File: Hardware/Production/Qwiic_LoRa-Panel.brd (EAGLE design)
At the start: 122.1 x 101.2 mm, 224 parts, among them J1 Qwiic Right Angle, J10 U.FL, J13 Qwiic Right Angle, J14 Qwiic Right Angle, J15 AVR_SPI_PROG_3X2TESTPOINTS, J16 U.FL, J19 Qwiic Right Angle, J2 Qwiic Right Angle, J20 Qwiic Right Angle, J21 AVR_SPI_PROG_3X2TESTPOINTS, J22 U.FL, J4 AVR_SPI_PROG_3X2TESTPOINTS, J5 U.FL, J7 Qwiic Right Angle, J8 Qwiic Right Angle, J9 AVR_SPI_PROG_3X2TESTPOINTS, U1 ATMEGA328P_TQFP, U2 RFM96W, U3 ATMEGA328P_TQFP, U4 RFM96W, U5 ATMEGA328P_TQFP, U6 RFM96W, U7 ATMEGA328P_TQFP, U8 RFM96W, Y1 16MHz, Y2 16MHz, Y3 16MHz, Y4 16MHz

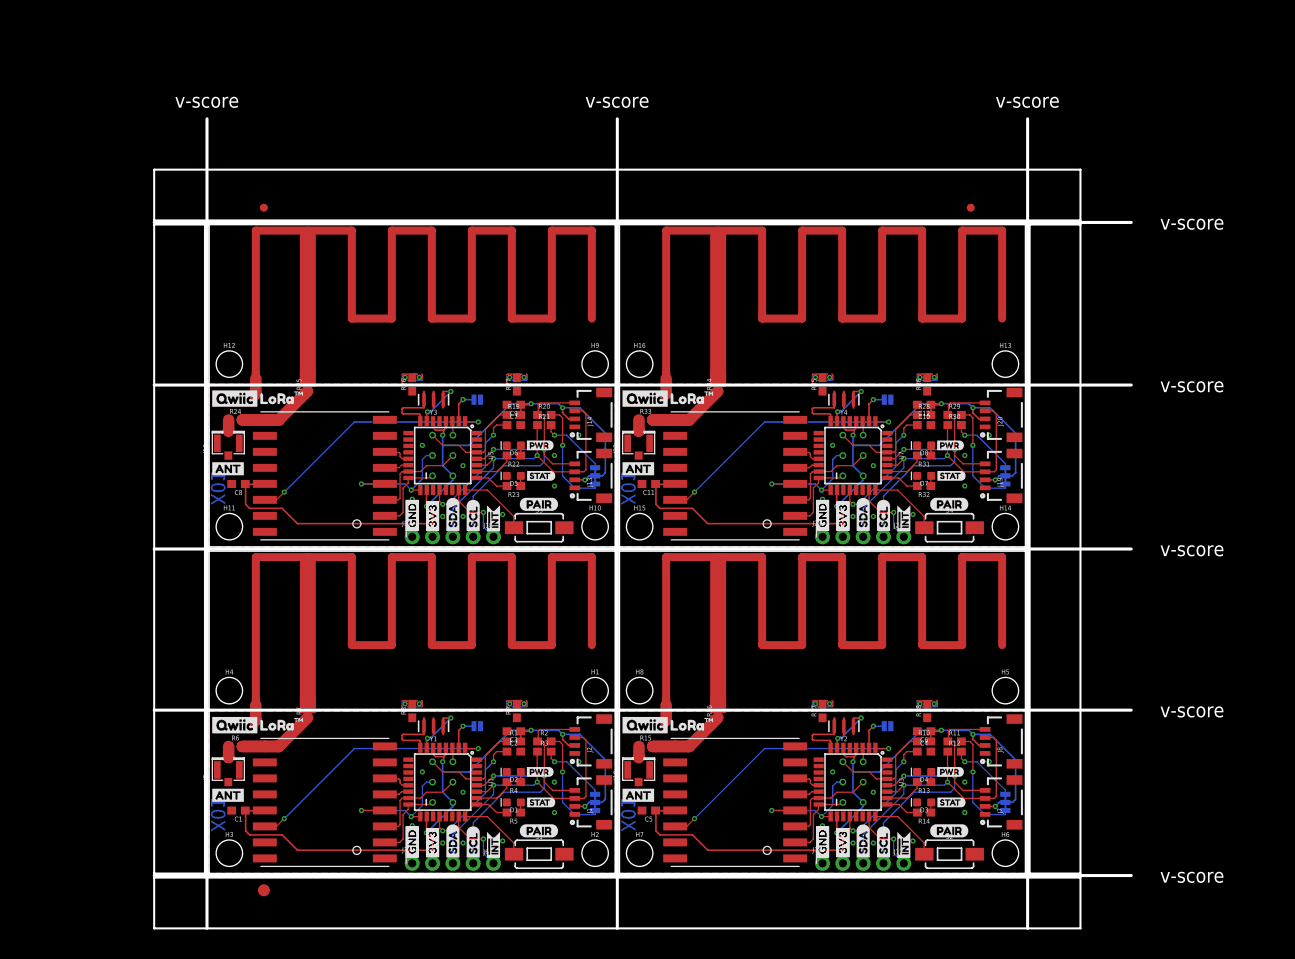
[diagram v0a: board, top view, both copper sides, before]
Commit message: x02
- Trim Antenna
- Silkscreen Changes to Comply with Semtech TM Requirements
- Adjust Mounting Holse to Mount to Qwiic Shield + Arduino R3
- Route DIO1 and DIO2 from RFM95
- Add Serial Debug Testpoints
- Add DNP for Shunt Components
- Add GND Leg Landing for Antenna Footprint
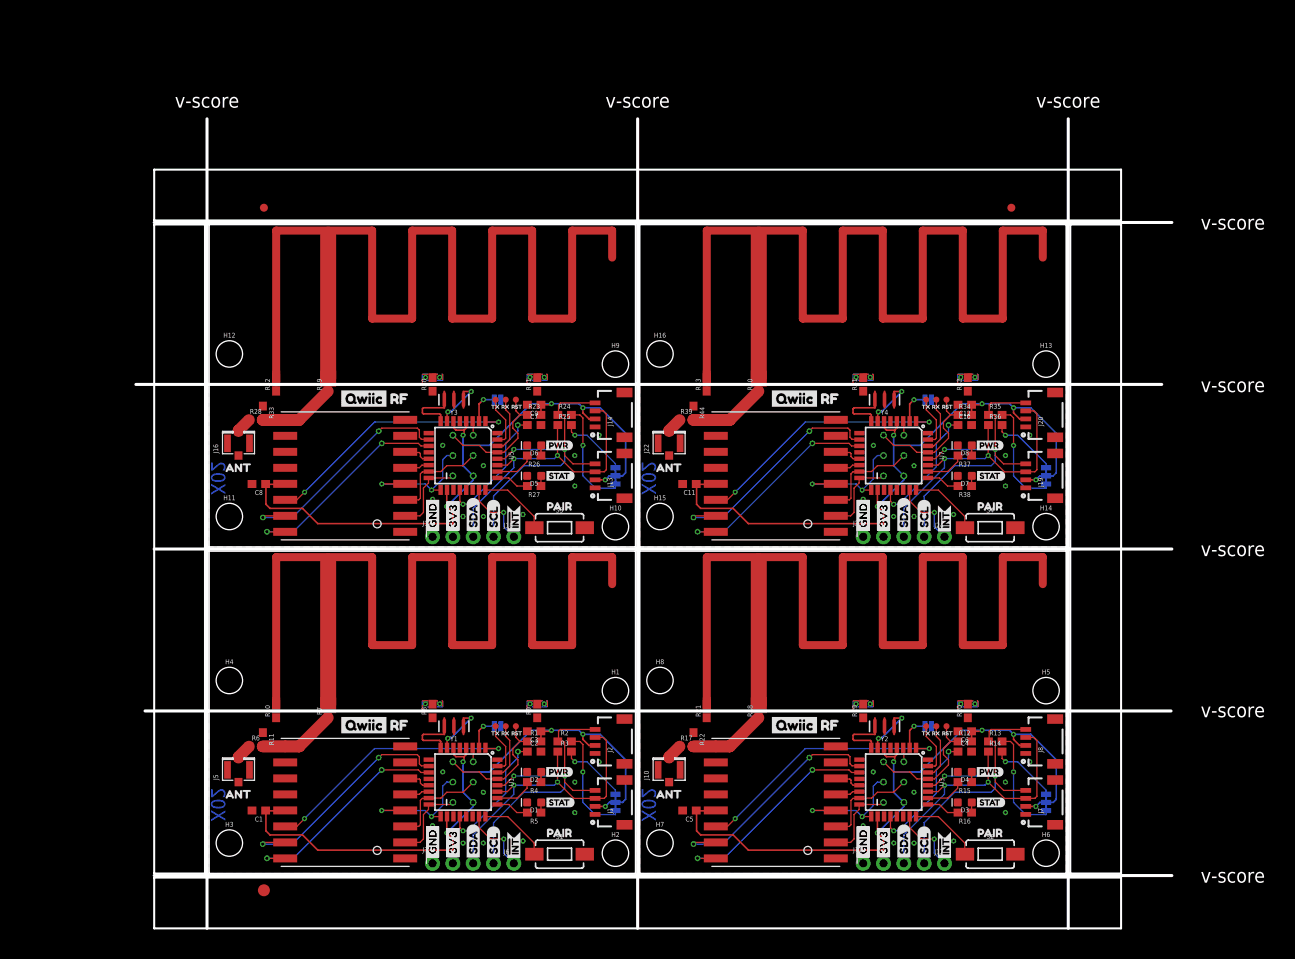
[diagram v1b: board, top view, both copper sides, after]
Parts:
- added R37, R38: 1k, SparkFun-Resistors:0603
- added R39, R44: DNP, SparkFun-Resistors:0603
- added R40, R41, R42, R43: 0, SparkFun-Resistors:0603
- added TP1, TP10, TP11, TP12, TP2, TP3, TP4, TP5, TP6, TP7, TP8, TP9: (no value), SparkFun-Connectors:PAD.03X.03
- added U$102: (no value), Labels:QWIIC-LOGO-SMALL
- added U$103: (no value), lora_mark#PNG (3):LORA_MARK#PNG
- added U$104: (no value), buzzard_labels (30):ANT0
- added U$105: (no value), buzzard_labels (30):PAIR1
- added U$106: (no value), buzzard_labels (32):TX1
- added U$107: (no value), buzzard_labels (32):RX0
- added U$108: (no value), buzzard_labels (32):RST2
- J15, J21, J4, J9: value AVR_SPI_PROG_3X2TESTPOINTS -> AVR_SPI_PROG
- R10, R19: value 10k -> 0
- R11: value 2.2k -> DNP
- R12: value 2.2k -> 10k
- R13, R14: value 1k -> 2.2k
- R15: value DNP -> 1k
- R16, R26, R27: value 0 -> 1k
- R17: value 0 -> DNP
- R20, R21, R29, R30: value 2.2k -> 0
- R22: value 1k -> DNP
- R23: value 1k -> 10k
- R24: value DNP -> 2.2k
- R25, R35, R36: value 0 -> 2.2k
- R28: value 10k -> DNP
- R31, R32: value 1k -> 0
- R34: value 0 -> 10k
- U$10: device lora_mark#PNG (2):LORA_MARK#PNG -> Labels:QWIIC-LOGO-SMALL
- U$101: device SparkFun-Aesthetics:PRODUCTION_INSTRUCTIONS -> buzzard_labels (29):RF1
- U$11: device Labels:QWIIC-LOGO-MEDIUM -> buzzard_labels (32):TX1
- U$15: device buzzard_labels (7):LORA0 -> buzzard_labels (29):RF1
- U$17: device buzzard_labels (7):TM1 -> lora_mark#PNG (3):LORA_MARK#PNG
- U$2: device buzzard_labels:ANT3 -> buzzard_labels (30):ANT0
- U$27: device Labels:SDA-[) -> buzzard_labels (32):RX0
- U$28: device Labels:SCL-[) -> buzzard_labels (32):RST2
- U$29, U$42: device Labels:GND-04 -> Labels:SDA-[)
- U$3: device buzzard_labels:PAIR0 -> buzzard_labels (30):PAIR1
- U$30, U$70: device Labels:3V3-04 -> Labels:SCL-[)
- U$31: device buzzard_labels:ANT3 -> Labels:GND-04
- U$32: device buzzard_labels:PAIR0 -> Labels:3V3-04
- U$35: device lora_mark#PNG (2):LORA_MARK#PNG -> buzzard_labels (1):QWIIC0
- U$36: device buzzard_labels (7):LORA0 -> SparkX:SPARKX-MEDIUM
- U$37: device buzzard_labels (1):QWIIC0 -> Labels:INT#-[<
- U$38: device buzzard_labels (7):TM1 -> Labels:GND-04
- U$39: device Labels:QWIIC-LOGO-MEDIUM -> Labels:GND-04
- U$40: device SparkX:SPARKX-MEDIUM -> Labels:3V3-04
- U$41: device Labels:INT#-[< -> Labels:3V3-04
- U$43: device Labels:GND-04 -> Labels:SCL-[)
- U$44: device Labels:3V3-04 -> Labels:INT#-[<
- U$45: device Labels:3V3-04 -> Labels:ADR-()
- U$46: device Labels:SDA-[) -> Labels:I_SUPER2_C-()-04
- U$47: device Labels:SCL-[) -> buzzard_labels (29):RF1
- U$48: device Labels:INT#-[< -> Labels:QWIIC-LOGO-SMALL
- U$49: device Labels:ADR-() -> lora_mark#PNG (3):LORA_MARK#PNG
- U$50: device Labels:I_SUPER2_C-()-04 -> buzzard_labels (30):ANT0
- U$51: value ANTENNA_915MHZ_INVERTED_F -> (none); device SparkX:ANTENNA_INVERTED_F_915MHZ -> buzzard_labels (30):PAIR1
- U$52: device Labels:SDA-[) -> buzzard_labels (32):TX1
- U$53: device Labels:SCL-[) -> buzzard_labels (32):RX0
- U$54: device Labels:GND-04 -> buzzard_labels (32):RST2
- U$55: value (none) -> ANTENNA_915MHZ_INVERTED_F; device Labels:3V3-04 -> SparkX:ANTENNA_INVERTED_F_915MHZ
- U$56: device buzzard_labels:ANT3 -> Labels:SDA-[)
- U$57: device buzzard_labels:PAIR0 -> Labels:SCL-[)
- U$58: device buzzard_labels:PWR1 -> Labels:GND-04
- U$59: device buzzard_labels:STAT2 -> Labels:3V3-04
- U$60: device lora_mark#PNG (2):LORA_MARK#PNG -> buzzard_labels:PWR1
- U$61: device buzzard_labels (7):LORA0 -> buzzard_labels:STAT2
- U$63: device buzzard_labels (7):TM1 -> SparkX:SPARKX-MEDIUM
- U$64: device Labels:QWIIC-LOGO-MEDIUM -> Labels:INT#-[<
- U$65: device SparkX:SPARKX-MEDIUM -> Labels:GND-04
- U$66: device Labels:INT#-[< -> Labels:GND-04
- U$67, U$68: device Labels:GND-04 -> Labels:3V3-04
- U$69: device Labels:3V3-04 -> Labels:SDA-[)
- U$71: device Labels:SDA-[) -> Labels:INT#-[<
- U$72: device Labels:SCL-[) -> Labels:ADR-()
- U$73: device Labels:INT#-[< -> Labels:I_SUPER2_C-()-04
- U$74: device Labels:ADR-() -> buzzard_labels (29):RF1
- U$75: device Labels:I_SUPER2_C-()-04 -> Labels:QWIIC-LOGO-SMALL
- U$76: value ANTENNA_915MHZ_INVERTED_F -> (none); device SparkX:ANTENNA_INVERTED_F_915MHZ -> lora_mark#PNG (3):LORA_MARK#PNG
- U$77: device Labels:SDA-[) -> buzzard_labels (30):ANT0
- U$78: device Labels:SCL-[) -> buzzard_labels (30):PAIR1
- U$79: device Labels:GND-04 -> buzzard_labels (32):TX1
- U$80: device Labels:3V3-04 -> buzzard_labels (32):RX0
- U$81: device buzzard_labels:ANT3 -> buzzard_labels (32):RST2
- U$82: value (none) -> ANTENNA_915MHZ_INVERTED_F; device buzzard_labels:PAIR0 -> SparkX:ANTENNA_INVERTED_F_915MHZ
- U$83: device buzzard_labels:PWR1 -> Labels:SDA-[)
- U$84: device buzzard_labels:STAT2 -> Labels:SCL-[)
- U$85: device lora_mark#PNG (2):LORA_MARK#PNG -> Labels:GND-04
- U$86: device buzzard_labels (7):LORA0 -> Labels:3V3-04
- U$87: device buzzard_labels (1):QWIIC0 -> buzzard_labels:PWR1
- U$88: device buzzard_labels (7):TM1 -> buzzard_labels:STAT2
- U$89: device Labels:QWIIC-LOGO-MEDIUM -> buzzard_labels (1):QWIIC0
- moved U$101 106.4 mm to (75.3, 59.4)
- moved U$51 104.3 mm to (95.1, 5.08)
- moved R11 86.5 mm to (6.73, 16.8), turned to 270 degrees
- moved R28 83.5 mm to (5.84, 56.7)
- moved R32 82.0 mm to (8.38, 61.1), turned to 90 degrees
- moved R10 81.1 mm to (8.38, 20.3), turned to 90 degrees
- moved U$77 81.1 mm to (1.14, 50.7), turned to 0 degrees
- moved R29 78.4 mm to (14.9, 61.1), turned to 90 degrees
- moved U$54 70.3 mm to (91.2, 17.5), turned to 0 degrees
- moved R30 65.5 mm to (27.9, 61.1), turned to 90 degrees
- moved R20 64.6 mm to (94.8, 20.3), turned to 90 degrees
- moved U$52 63.2 mm to (88.6, 17.5), turned to 0 degrees
- moved U$53 62.1 mm to (89.9, 17.5), turned to 0 degrees
- moved R19 57.2 mm to (81.8, 20.3), turned to 90 degrees
- moved U$76 55.0 mm to (2.67, 59.2), flipped to the bottom
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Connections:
- removed net N$10 (its old number): R6.2, R7.1
- new net N$11: R10.2, U$1.GND
- new net RFM_DIO1: U1.10, U2.DIO1
- new net RFM_DIO2: U1.11, U2.DIO2
- new net RFM_DIO3: U3.10, U4.DIO1
- new net RFM_DIO4: U3.11, U4.DIO2
- new net RFM_DIO5: U5.10, U6.DIO1
- new net RFM_DIO6: U5.11, U6.DIO2
- new net RFM_DIO7: U7.10, U8.DIO1
- new net RFM_DIO8: U7.11, U8.DIO2
- new net RX: TP1.P$1, U1.30
- new net RX1: TP4.P$1, U3.30
- new net RX2: TP7.P$1, U5.30
- new net RX3: TP10.P$1, U7.30
- new net TX: TP2.P$1, U1.31
- new net TX1: TP5.P$1, U3.31
- new net TX2: TP8.P$1, U5.31
- new net TX3: TP11.P$1, U7.31
- net 3.3V1: now also R12.2; no longer R10.2
- net 3.3V2: now also R23.2; no longer R19.2
- net 3.3V3: now also R34.2; no longer R28.2
- net ANCHOR3: now also R19.2; no longer R17.2
- net ANCHOR4: now also R20.2; no longer R18.2
- net ANCHOR5: now also R30.2; no longer R26.2
- net ANCHOR6: now also R31.2; no longer R27.2
- net ANCHOR7: now also R41.2; no longer R35.2
- net ANCHOR8: now also R42.2; no longer R36.2
- net ANT: now also R11.2, R6.2, R7.1
- net ANT1: now also R17.2, R18.1, R22.2
- net ANT2: now also R28.2, R29.1, R33.2
- net ANT3: now also R39.2, R40.1, R44.2
- net GND: now also R10.1, R11.1; no longer U$1.GND
- net GND1: now also R19.1, R20.1, R21.1, R22.1; no longer R17.1, R18.1, U$26.GND
- net GND2: now also R30.1, R31.1, R32.1, R33.1; no longer R26.1, R27.1, U$51.GND
- net GND3: now also R41.1, R42.1, R43.1, R44.1; no longer R35.1, R36.1, U$76.GND
- net N$13: now also R14.2; no longer R12.2
- net N$14: now also R13.2; no longer R11.2
- net N$15: now also R15.1; no longer R13.1
- net N$16: now also R16.1; no longer R14.1
- net N$17: now also R17.1; no longer R15.1
- net N$19: now also R18.2; no longer R16.2
- net N$20: now also R21.2, U$26.GND; no longer R15.2, R16.1
- net N$23: now also R25.2; no longer R21.2
- net N$24: now also R24.2; no longer R20.2
- net N$25: now also R26.1; no longer R22.1
- net N$26: now also R27.1; no longer R23.1
- net N$27: now also R28.1; no longer R24.1
- net N$29: now also R29.2, U$55.FEED; no longer R25.2, U$51.FEED
- net N$30: now also R32.2, U$55.GND; no longer R24.2, R25.1
- net N$33: now also R36.2; no longer R30.2
- net N$34: now also R35.2; no longer R29.2
- net N$35: now also R37.1; no longer R31.1
- net N$36: now also R38.1; no longer R32.1
- net N$37: now also R39.1; no longer R33.1
- net N$39: now also R40.2, U$82.FEED; no longer R34.2, U$76.FEED
- net N$40: now also R43.2, U$82.GND; no longer R33.2, R34.1
- net PAIR_LED1: now also R16.2; no longer R14.2
- net PAIR_LED2: now also R27.2; no longer R23.2
- net PAIR_LED3: now also R38.2; no longer R32.2
- net PWR_LED1: now also R15.2; no longer R13.2
- net PWR_LED2: now also R26.2; no longer R22.2
- net PWR_LED3: now also R37.2; no longer R31.2
- net RST: now also TP3.P$1
- net RST1: now also R12.1, TP6.P$1; no longer R10.1
- net RST2: now also R23.1, TP9.P$1; no longer R19.1
- net RST3: now also R34.1, TP12.P$1; no longer R28.1
- net SCL1: now also R13.1; no longer R11.1
- net SCL2: now also R24.1; no longer R20.1
- net SCL3: now also R35.1; no longer R29.1
- net SDA1: now also R14.1; no longer R12.1
- net SDA2: now also R25.1; no longer R21.1
- net SDA3: now also R36.1; no longer R30.1
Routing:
- net RFM_DIO7: track 0.00 -> 29.3 mm, vias 0 -> 2
- net RFM_DIO5: track 0.00 -> 29.3 mm, vias 0 -> 2
- net RFM_DIO3: track 0.00 -> 29.3 mm, vias 0 -> 2
- net RFM_DIO1: track 0.00 -> 29.3 mm, vias 0 -> 2
- net RFM_DIO8: track 0.00 -> 27.2 mm, vias 0 -> 2
- net RFM_DIO4: track 0.00 -> 27.2 mm, vias 0 -> 2
- net RFM_DIO6: track 0.00 -> 27.2 mm, vias 0 -> 2
- net RFM_DIO2: track 0.00 -> 27.2 mm, vias 0 -> 2
- net ANT3: track 4.57 -> 14.3 mm
- net ANT1: track 4.57 -> 14.3 mm
- net ANT2: track 4.57 -> 14.3 mm
- net ANT: track 4.57 -> 14.3 mm
- net N$10 (its old number): track 9.66 -> 0.00 mm
- net N$30: track 9.66 -> 0.12 mm
- net N$40: track 9.66 -> 0.12 mm
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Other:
- board size 122.1 x 101.2 mm -> 129.5 x 101.2 mm
- board text added: "X02"
- board text removed: "0.8mm Thickness PCB"
- board text removed: "X01"

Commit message: Version X03
Add Chip Select pullup on the radio module, only affects programming.
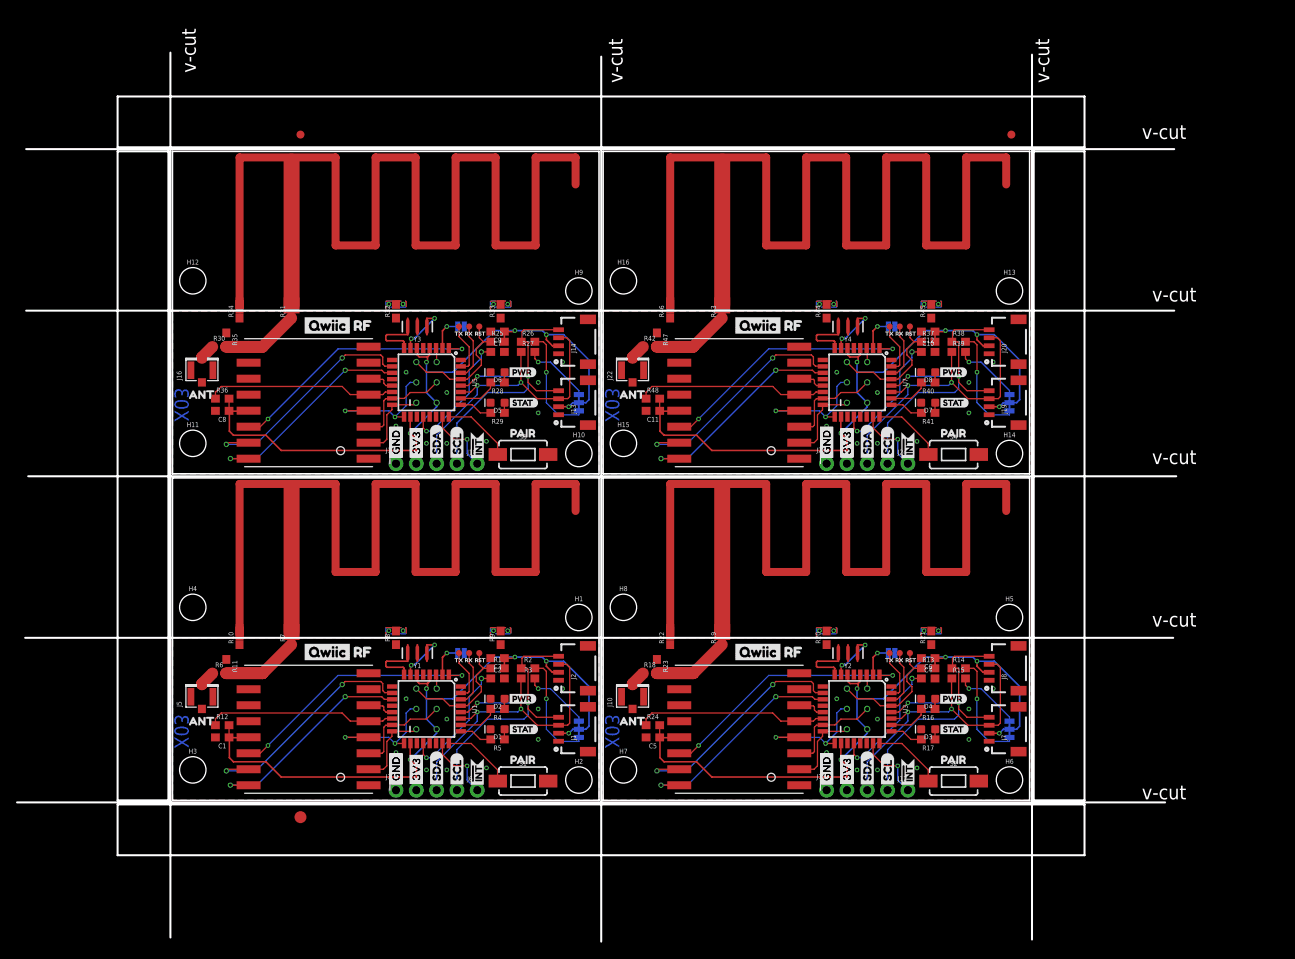
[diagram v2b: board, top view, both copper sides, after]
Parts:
- added R45, R46: 0, SparkFun-Resistors:0603
- added R47: DNP, SparkFun-Resistors:0603
- added R48: 10k, SparkFun-Resistors:0603
- R13, R24, R25, R36: value 2.2k -> 10k
- R15, R26, R27, R38: value 1k -> 2.2k
- R17, R28: value DNP -> 1k
- R18, R30, R42: value 0 -> DNP
- R22, R33, R44: value DNP -> 0
- R23: value 10k -> DNP
- R29, R40, R41: value 0 -> 1k
- R34: value 10k -> 0
- R35: value 2.2k -> DNP
- R37: value 1k -> 10k
- R39: value DNP -> 2.2k
- moved R36 96.7 mm to (1.65, 59.4)
- moved R35 96.6 mm to (2.16, 66.7), turned to 270 degrees
- moved R12 92.8 mm to (1.65, 18.5)
- moved R34 91.6 mm to (3.81, 70.3), turned to 90 degrees
- moved R24 40.3 mm to (55.5, 18.5)
- moved R42 40.0 mm to (55.1, 65.8), turned to 0 degrees
- moved R39 35.1 mm to (93.7, 65.2)
- moved R23 35.0 mm to (56.0, 25.9), turned to 270 degrees
- moved R33 32.3 mm to (36.4, 70.3), turned to 90 degrees
- moved R31 32.1 mm to (10.3, 70.3)
- moved R28 30.6 mm to (36.1, 61.4), turned to 180 degrees
- moved R17 30.2 mm to (89.9, 16.8), turned to 180 degrees
- moved R21 29.5 mm to (90.3, 29.5)
- moved R30 27.1 mm to (1.27, 65.8), turned to 0 degrees
- moved R29 21.5 mm to (36.1, 57.6), turned to 180 degrees
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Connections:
- net 3.3V: now also R12.2
- net 3.3V1: now also R13.2, R24.2; no longer R12.2
- net 3.3V2: now also R25.2, R36.2; no longer R23.2
- net 3.3V3: now also R37.2, R48.2; no longer R34.2
- net ANCHOR3: now also R20.2; no longer R19.2
- net ANCHOR4: now also R21.2; no longer R20.2
- net ANCHOR5: now also R32.2; no longer R30.2
- net ANCHOR6: now also R33.2; no longer R31.2
- net ANCHOR7: now also R44.2; no longer R41.2
- net ANCHOR8: now also R45.2; no longer R42.2
- net ANT1: now also R18.2, R19.1, R23.2; no longer R17.2, R18.1, R22.2
- net ANT2: now also R30.2, R31.1, R35.2; no longer R28.2, R29.1, R33.2
- net ANT3: now also R42.2, R43.1, R47.2; no longer R39.2, R40.1, R44.2
- net GND1: now also R23.1; no longer R19.1
- net GND2: now also R34.1, R35.1; no longer R30.1, R31.1
- net GND3: now also R45.1, R46.1, R47.1; no longer R41.1, R42.1, R43.1
- net N$13: now also R15.2; no longer R14.2
- net N$14: now also R14.2; no longer R13.2
- net N$15: now also R16.1; no longer R15.1
- net N$16: now also R17.1; no longer R16.1
- net N$17: now also R18.1; no longer R17.1
- net N$19: now also R19.2; no longer R18.2
- net N$20: now also R22.2; no longer R21.2
- net N$23: now also R27.2; no longer R25.2
- net N$24: now also R26.2; no longer R24.2
- net N$25: now also R28.1; no longer R26.1
- net N$26: now also R29.1; no longer R27.1
- net N$27: now also R30.1; no longer R28.1
- net N$29: now also R31.2; no longer R29.2
- net N$30: now also R34.2; no longer R32.2
- net N$33: now also R39.2; no longer R36.2
- net N$34: now also R38.2; no longer R35.2
- net N$35: now also R40.1; no longer R37.1
- net N$36: now also R41.1; no longer R38.1
- net N$37: now also R42.1; no longer R39.1
- net N$39: now also R43.2; no longer R40.2
- net N$40: now also R46.2; no longer R43.2
- net PAIR_LED1: now also R17.2; no longer R16.2
- net PAIR_LED2: now also R29.2; no longer R27.2
- net PAIR_LED3: now also R41.2; no longer R38.2
- net PWR_LED1: now also R16.2; no longer R15.2
- net PWR_LED2: now also R28.2; no longer R26.2
- net PWR_LED3: now also R40.2; no longer R37.2
- net RFM_CS: now also R12.1
- net RFM_CS1: now also R24.1
- net RFM_CS2: now also R36.1
- net RFM_CS3: now also R48.1
- net RST1: now also R13.1; no longer R12.1
- net RST2: now also R25.1; no longer R23.1
- net RST3: now also R37.1; no longer R34.1
- net SCL1: now also R14.1; no longer R13.1
- net SCL2: now also R26.1; no longer R24.1
- net SCL3: now also R38.1; no longer R35.1
- net SDA1: now also R15.1; no longer R14.1
- net SDA2: now also R27.1; no longer R25.1
- net SDA3: now also R39.1; no longer R36.1
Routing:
- net RFM_CS: track 3.08 -> 23.8 mm
- net RFM_CS2: track 3.08 -> 23.8 mm
- net RFM_CS1: track 3.08 -> 23.8 mm
- net RFM_CS3: track 3.08 -> 23.8 mm
- net 3.3V2: track 88.8 -> 90.3 mm
- net 3.3V3: track 88.8 -> 90.3 mm
- net 3.3V1: track 88.8 -> 90.3 mm
- net 3.3V: track 88.8 -> 90.3 mm
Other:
- board size 129.5 x 101.2 mm -> 144.9 x 111.1 mm
- board text added: "RFM95W 915MHz"
- board text added: "X03"
- board text added: "v-cut"
- board text removed: "X02"
- board text removed: "v-score"
